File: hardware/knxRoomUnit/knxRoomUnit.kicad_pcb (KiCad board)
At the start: 4 copper layers, 65 x 42 mm, 88 parts, among them J1 esp_prog, J2 JTAG, J3 KNX, P1 ePaper, P2 ePaper FL, Q1 S8050, Q2 S8050, Q3 SI1308, SW1 rst, SW2 knx_prog, SW3 ui_up, SW4 ui_dw, SW5 ui_ok, U1 ESP32-WROOM-32, U2 BME280, U3 VCNL4040M3OE, U4 NCN5130MNTWG, Y1 830055951 16MHz

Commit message: Initial hardware commit
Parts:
- removed C10: 1uF, Capacitor_SMD:C_0603_1608Metric
- removed C11: 10uF, Capacitor_SMD:C_0603_1608Metric
- removed the C12 at (126.5, 70.0)
- removed the C13 at (110.9, 71.5)
- removed the C14 at (110.9, 65.2)
- removed C4: 47nF, Capacitor_SMD:C_0603_1608Metric
- removed C5, C7, C8: 100nF, Capacitor_SMD:C_0603_1608Metric
- removed C6: 220nF, Capacitor_SMD:C_0603_1608Metric
- removed C9: 47uF, Capacitor_SMD:C_Elec_6.3x5.4
- removed D2: SS16, Diode_SMD:D_SMA
- removed the D3 at (142.9, 65.5)
- removed the J2 at (113.6, 46.6)
- removed JP1: UC2, Jumper:SolderJumper-3_P1.3mm_Bridged12_Pad1.0x1.5mm
- removed JP2: UC1, Jumper:SolderJumper-3_P1.3mm_Bridged12_Pad1.0x1.5mm
- removed L1: 220uH, Inductor_SMD:L_Wuerth_MAPI-3020
- removed the R11 at (115.5, 75.9)
- removed the R12 at (123.4, 65.8)
- removed the R13 at (114.2, 62.3)
- removed the R14 at (109.5, 73.6)
- removed the R15 at (109.5, 77.0)
- removed the R16 at (116.3, 62.3)
- removed the R17 at (118.5, 62.3)
- removed Y1: 830055951 16MHz, WE-XTAL:WE-XTAL_CFPX-180
- added GN1: OpenKNX_BCU, OpenKNX:NanoBCU_PinHeader_SMD_low_profile, F.Cu at (128.1, 74.3)
- added R23: 8.2k, Resistor_SMD:R_0603_1608Metric, F.Cu at (83.1, 68.3)
- D3: renamed from D1; value ui_led -> UI
- J1: renamed from J3; footprint Ettinger:13.14.125 -> OpenKNX:KNX_Connector
- J2: renamed from J1; value esp_prog -> PROG
- R10: renamed from R3; footprint Resistor_SMD:R_0402_1005Metric -> Resistor_SMD:R_0603_1608Metric
- R11: renamed from R1; footprint Resistor_SMD:R_0402_1005Metric -> Resistor_SMD:R_0603_1608Metric
- R12: renamed from R4; footprint Resistor_SMD:R_0402_1005Metric -> Resistor_SMD:R_0603_1608Metric
- R13: renamed from R8; footprint Resistor_SMD:R_0402_1005Metric -> Resistor_SMD:R_0603_1608Metric
- R14: renamed from R5; footprint Resistor_SMD:R_0402_1005Metric -> Resistor_SMD:R_0603_1608Metric
- R15: renamed from R6; footprint Resistor_SMD:R_0402_1005Metric -> Resistor_SMD:R_0603_1608Metric
- R16: renamed from R9; footprint Resistor_SMD:R_0402_1005Metric -> Resistor_SMD:R_0603_1608Metric
- R17: renamed from R10; footprint Resistor_SMD:R_0402_1005Metric -> Resistor_SMD:R_0603_1608Metric
- R18: renamed from R7; footprint Resistor_SMD:R_0402_1005Metric -> Resistor_SMD:R_0603_1608Metric
- R19: renamed from R18; footprint Resistor_SMD:R_0402_1005Metric -> Resistor_SMD:R_0603_1608Metric
- R20: renamed from R19; footprint Resistor_SMD:R_0402_1005Metric -> Resistor_SMD:R_0603_1608Metric
- R21: renamed from R20; footprint Resistor_SMD:R_0402_1005Metric -> Resistor_SMD:R_0603_1608Metric
- R22: renamed from R21; footprint Resistor_SMD:R_0402_1005Metric -> Resistor_SMD:R_0603_1608Metric
- R24: renamed from R22; footprint Resistor_SMD:R_0402_1005Metric -> Resistor_SMD:R_0603_1608Metric
- R25: renamed from R23; footprint Resistor_SMD:R_0402_1005Metric -> Resistor_SMD:R_0603_1608Metric
- R26: renamed from R24; footprint Resistor_SMD:R_0402_1005Metric -> Resistor_SMD:R_0603_1608Metric
- R30: renamed from R26; footprint Resistor_SMD:R_0402_1005Metric -> Resistor_SMD:R_0603_1608Metric
- R31: renamed from R27; footprint Resistor_SMD:R_0402_1005Metric -> Resistor_SMD:R_0603_1608Metric
- R9: renamed from R2; footprint Resistor_SMD:R_0402_1005Metric -> Resistor_SMD:R_0603_1608Metric
- SW2: renamed from SW3; value ui_up -> UI_UP
- SW3: renamed from SW2; value knx_prog -> KNX_PROG
- SW4: value ui_dw -> UI_DW
- SW5: value ui_ok -> UI_OK
- U4: value NCN5130MNTWG -> SHT31-DIS; footprint ON_Semiconductor:CASE485AU−01 -> Sensor_Humidity:Sensirion_DFN-8-1EP_2.5x2.5mm_P0.5mm_EP1.1x1.7mm
- moved U4 34.5 mm to (83.9, 65.3), turned to 0 degrees
- moved J1 5.31 mm to (147.0, 71.6), turned to 0 degrees
- moved C22 3.75 mm to (115.5, 49.5)
- moved C24 3.75 mm to (113.0, 49.5)
- moved C25 3.75 mm to (110.5, 49.5)
- moved C26 3.75 mm to (115.5, 53.9)
- moved C28 3.75 mm to (113.0, 53.9)
- moved C30 3.75 mm to (110.5, 53.9)
- moved R1 3.75 mm to (120.3, 58.4), turned to 180 degrees
- moved R18 2.66 mm to (132.2, 38.4)
- moved D3 2.60 mm to (129.0, 38.4)
- moved C14 2.28 mm to (138.3, 38.4)
- moved R11 2.25 mm to (135.3, 38.4)
- moved C13 2.19 mm to (141.4, 38.4), turned to 0 degrees
- moved C12 1.59 mm to (144.4, 38.4), turned to 0 degrees
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- renumbered C1 to C12, C2 to C13, C3 to C14, C24 to C20, C25 to C22, C20 to C23, C26 to C24, C27 to C25, C28 to C26, C22 to C27, C29 to C28, C23 to C29, P2 to P1, P1 to P2, R30 to R1, R28 to R27, R29 to R28, R25 to R29, U1 to U2, U2 to U3, U3 to U5
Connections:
- P1 pad 2: (no net) -> unconnected-(P1-Pin_2-Pad2)
- P1 pad 3: (no net) -> unconnected-(P1-Pin_3-Pad3)
- P1 pad 4: (no net) -> unconnected-(P1-Pin_4-Pad4)
- P2 pad 1: (no net) -> unconnected-(P2-Pin_1-Pad1)
- P2 pad 6: (no net) -> unconnected-(P2-Pin_6-Pad6)
- P2 pad 7: (no net) -> unconnected-(P2-Pin_7-Pad7)
- U2 pad 13: JTAG_TMS -> unconnected-(U2-IO14-Pad13)
- U2 pad 14: JTAG_TDI -> unconnected-(U2-IO12-Pad14)
- U2 pad 16: JTAG_TCK -> unconnected-(U2-IO13-Pad16)
- U2 pad 17: (no net) -> unconnected-(U2-SHD/SD2-Pad17)
- U2 pad 18: (no net) -> unconnected-(U2-SWP/SD3-Pad18)
- U2 pad 19: (no net) -> unconnected-(U2-SCS/CMD-Pad19)
- U2 pad 20: (no net) -> unconnected-(U2-SCK/CLK-Pad20)
- U2 pad 21: (no net) -> unconnected-(U2-SDO/SD0-Pad21)
- U2 pad 22: (no net) -> unconnected-(U2-SDI/SD1-Pad22)
- U2 pad 23: JTAG_TDO -> KNX_SAVE
- U2 pad 32: (no net) -> unconnected-(U2-NC-Pad32)
- U2 pad 4: (no net) -> unconnected-(U2-SENSOR_VP-Pad4)
- U2 pad 5: (no net) -> unconnected-(U2-SENSOR_VN-Pad5)
- U4 pad 1: GND -> unconnected-(U4-SDA-Pad1)
- U4 pad 2: GND -> unconnected-(U4-ADDR-Pad2)
- U4 pad 3: /KNX/TXO -> unconnected-(U4-ALERT-Pad3)
- U4 pad 4: /KNX/CCP -> unconnected-(U4-SCL-Pad4)
- U4 pad 5: /KNX/CAV -> unconnected-(U4-VDD-Pad5)
- U4 pad 6: /KNX/VBUS1 -> unconnected-(U4-~{RESET}-Pad6)
- U4 pad 7: /KNX/CEQ1 -> unconnected-(U4-R-Pad7)
- U4 pad 8: /KNX/CEQ2 -> Net-(U4-VSS-Pad8)
- U4 pad 9: /KNX/VFILT -> Net-(U4-VSS-Pad8)
- U5 pad 3: Net-(C17-Pad1) -> Net-(R23-Pad2)
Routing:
- net Net-(U2-IO35): track 0.00 -> 33.2 mm, vias 0 -> 1
- net ESP_RX: track 0.00 -> 31.4 mm, vias 0 -> 1
- net ESP_TX: track 0.00 -> 31.0 mm, vias 0 -> 1
- net +3V3: track 0.00 -> 29.1 mm, vias 0 -> 2
- net ESP_EN: track 0.00 -> 28.8 mm, vias 0 -> 2
- net KNX_RX: track 0.00 -> 22.7 mm
- net KNX_SAVE: track 0.00 -> 22.5 mm, vias 0 -> 2
- net KNX_TX: track 0.00 -> 19.8 mm
- net Net-(GN1-KNX+): track 0.00 -> 19.2 mm
- net Net-(J2-Pin_5): track 0.00 -> 11.3 mm, vias 0 -> 2
- net Net-(J2-Pin_4): track 0.00 -> 7.53 mm
- net Net-(U2-IO32): track 0.00 -> 5.72 mm
- net I2C_SDA: track 0.00 -> 4.28 mm
- net I2C_SCK: track 0.00 -> 4.14 mm
- net VCNL4040_INT: track 0.00 -> 3.92 mm
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- added copper zone on B.Cu, net GND
- added copper zone on F.Cu, net GND

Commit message: Hardware Update
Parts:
- moved C25 5.01 mm to (115.5, 49.5)
- moved C22 4.89 mm to (110.6, 49.5)
- moved R26 1.03 mm to (136.4, 63.1), turned to 90 degrees
- moved R10 0.74 mm to (121.5, 49.6)
- moved R12 0.55 mm to (142.7, 63.1), turned to 90 degrees
- moved R14 0.50 mm to (139.0, 63.1), turned to 90 degrees
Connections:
- R13 pad 2: Net-(R13-Pad2) -> Net-(U2-IO35)
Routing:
- net /ePaper/PREVGL: track 0.00 -> 30.6 mm
- net Net-(P2-Pin_5): track 0.00 -> 20.7 mm, vias 0 -> 2
- net +3V3: track 29.1 -> 48.8 mm
- net Net-(P2-Pin_4): track 0.00 -> 18.8 mm, vias 0 -> 2
- net Net-(P2-Pin_19): track 0.00 -> 17.6 mm, vias 0 -> 2
- net Net-(C19-Pad1): track 0.00 -> 17.5 mm
- net Net-(P2-Pin_20): track 0.00 -> 17.3 mm, vias 0 -> 2
- net Net-(P2-Pin_22): track 0.00 -> 16.7 mm, vias 0 -> 2
- net /ePaper/PREVGH: track 0.00 -> 13.5 mm
- net Net-(P2-Pin_24): track 0.00 -> 12.2 mm
- net Net-(P2-Pin_18): track 0.00 -> 12.2 mm, vias 0 -> 2
- net Net-(P1-Pin_1): track 0.00 -> 11.7 mm
- net Net-(D6-A): track 0.00 -> 9.93 mm
- net /ePaper/RESE: track 0.00 -> 9.92 mm
- net /ePaper/GDR: track 0.00 -> 8.83 mm
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
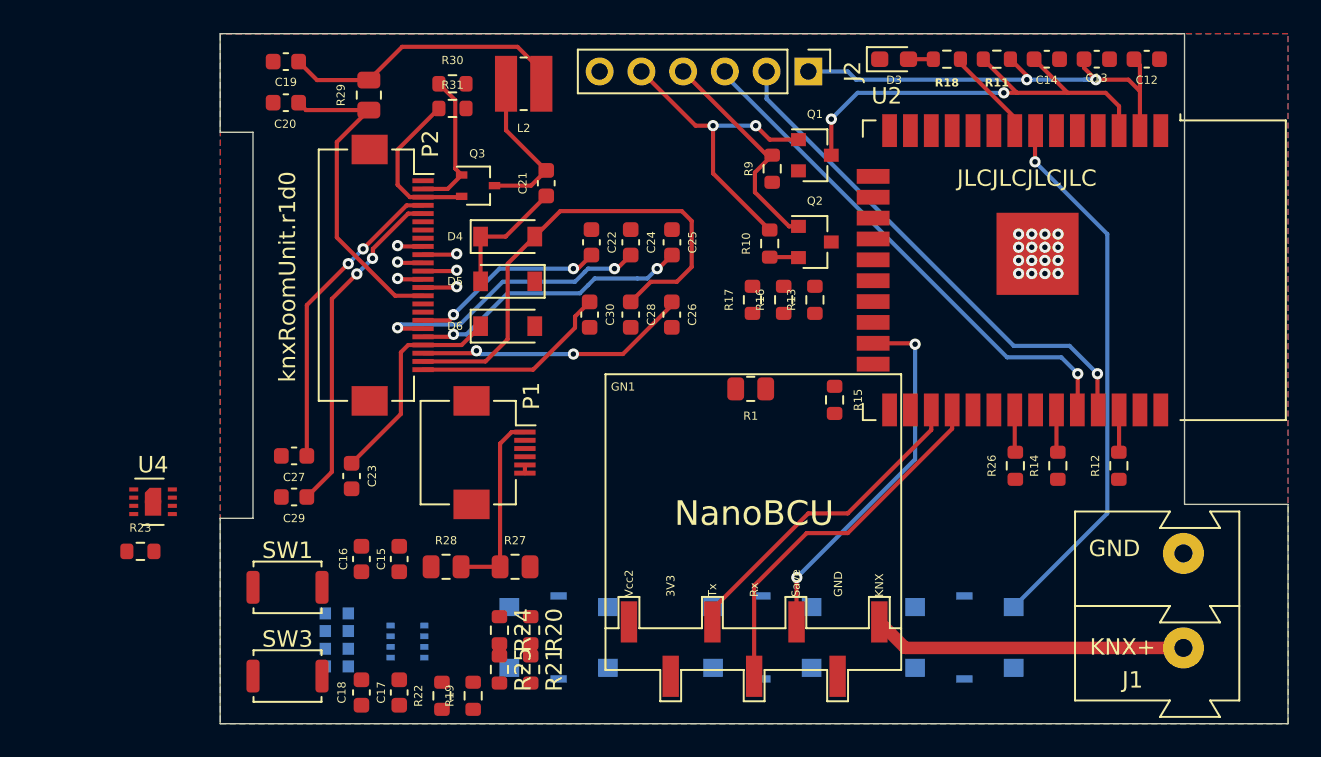
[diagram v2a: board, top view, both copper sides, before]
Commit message: Updated sensors
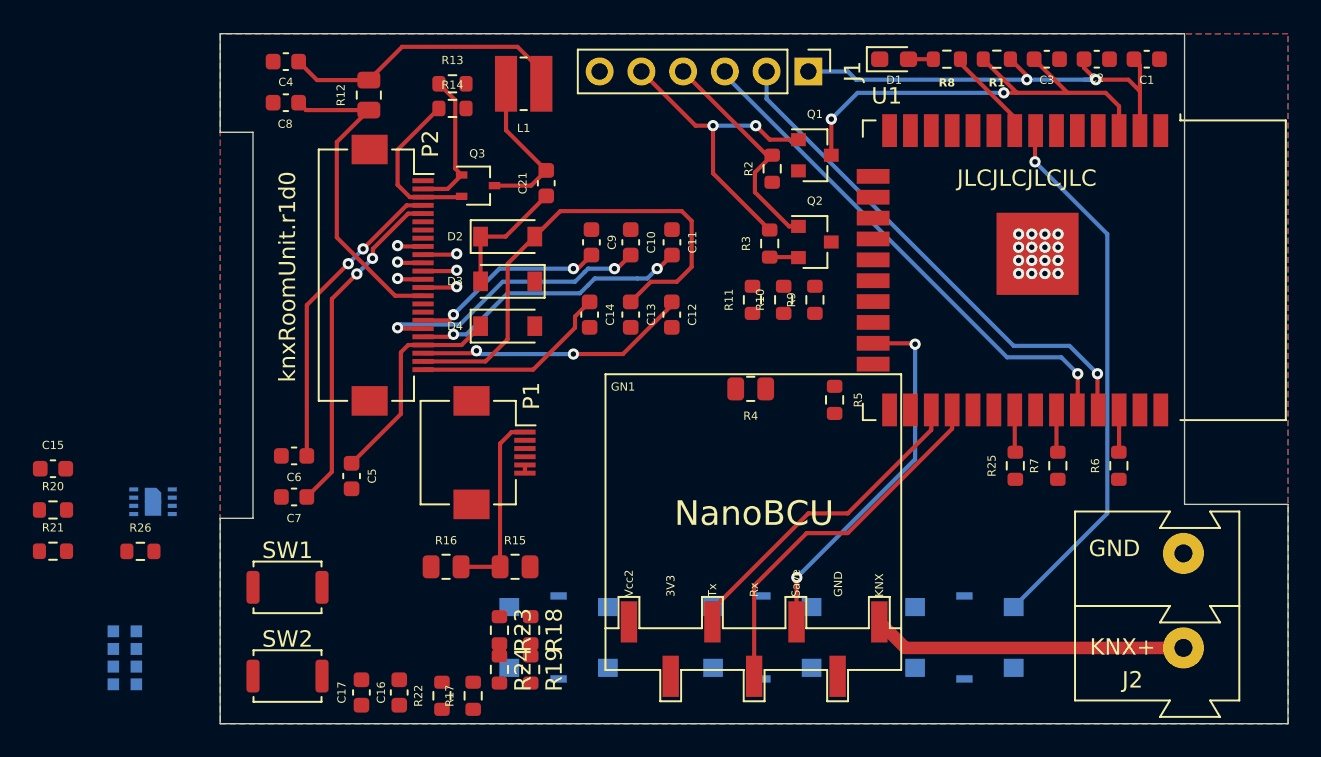
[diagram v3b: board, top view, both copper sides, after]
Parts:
- removed the C16 at (96.6, 68.8)
- removed U5: VCNL4040M3OE, libs:VISHAY_VCNL4040_4X2X1.1
- added R20: 0, Resistor_SMD:R_0603_1608Metric, F.Cu at (77.8, 65.8)
- added R21: 2.2k, Resistor_SMD:R_0603_1608Metric, F.Cu at (77.8, 68.3)
- U2: renamed from U4; moved to B.Cu
- U3: value BME280 -> VCNL4040M3OE; footprint Package_LGA:Bosch_LGA-8_2.5x2.5mm_P0.65mm_ClockwisePinNumbering -> VCNL4040M3OE:VISHAY_VCNL4040_4X2X1.1
- moved C15 21.8 mm to (77.8, 63.3), turned to 0 degrees
- moved U3 17.2 mm to (82.2, 74.8), turned to 180 degrees
- turned U2 to 180 degrees
- renumbered C12 to C1, C24 to C10, C25 to C11, C26 to C12, C28 to C13, C30 to C14, C17 to C16, C18 to C17, C13 to C2, C14 to C3, C19 to C4, C23 to C5, C27 to C6, C29 to C7, C20 to C8, C22 to C9, D3 to D1, D4 to D2, D5 to D3, D6 to D4, J2 to J1, J1 to J2, L2 to L1, R11 to R1, R16 to R10, R17 to R11, R29 to R12, R30 to R13, R31 to R14, R27 to R15, R28 to R16, R19 to R17, R20 to R18, R21 to R19, R9 to R2, R24 to R23, R25 to R24, R26 to R25, R23 to R26, R10 to R3, R1 to R4, R15 to R5, R12 to R6, R14 to R7, R18 to R8, R13 to R9, SW3 to SW2, SW2 to SW3, U2 to U1
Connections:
- C15 pad 1: Net-(U3-CSB) -> Net-(U2-VDD)
- C16 pad 1: Net-(C17-Pad1) -> Net-(C16-Pad1)
- C17 pad 1: Net-(C17-Pad1) -> Net-(C16-Pad1)
- R10 pad 2: Net-(U2-IO34) -> Net-(U1-IO34)
- R11 pad 2: Net-(U2-IO33) -> Net-(U1-IO33)
- R17 pad 2: Net-(U3-CSB) -> Net-(U2-VDD)
- R18 pad 1: Net-(U3-SCK) -> Net-(U2-SCL)
- R19 pad 1: Net-(U3-SDI) -> Net-(U2-SDA)
- R22 pad 2: Net-(C17-Pad1) -> Net-(C16-Pad1)
- R23 pad 1: Net-(R24-Pad1) -> Net-(R23-Pad1)
- R24 pad 1: Net-(R25-Pad1) -> Net-(R24-Pad1)
- R25 pad 1: Net-(R26-Pad1) -> Net-(R25-Pad1)
- R26 pad 1: Net-(C17-Pad1) -> Net-(C16-Pad1)
- R26 pad 2: Net-(R23-Pad2) -> Net-(R26-Pad2)
- R9 pad 2: Net-(U2-IO35) -> Net-(U1-IO35)
- U1 pad 6: Net-(U2-IO34) -> Net-(U1-IO34)
- U1 pad 7: Net-(U2-IO35) -> Net-(U1-IO35)
- U1 pad 9: Net-(U2-IO33) -> Net-(U1-IO33)
- U2 pad 1: unconnected-(U4-SDA-Pad1) -> Net-(U2-SDA)
- U2 pad 2: unconnected-(U4-ADDR-Pad2) -> GND
- U2 pad 3: unconnected-(U4-ALERT-Pad3) -> Net-(U2-ALERT)
- U2 pad 4: unconnected-(U4-SCL-Pad4) -> Net-(U2-SCL)
- U2 pad 5: unconnected-(U4-VDD-Pad5) -> Net-(U2-VDD)
- U2 pad 6: unconnected-(U4-~{RESET}-Pad6) -> Net-(U2-~{RESET})
- U2 pad 7: unconnected-(U4-R-Pad7) -> GND
- U2 pad 8: Net-(U4-VSS-Pad8) -> GND
- U2 pad 9: Net-(U4-VSS-Pad8) -> GND
- U3 pad 2: Net-(U3-CSB) -> Net-(U3-Pad2)
- U3 pad 3: Net-(U3-SDI) -> Net-(R26-Pad2)
- U3 pad 4: Net-(U3-SCK) -> Net-(C16-Pad1)
- U3 pad 5: GND -> Net-(U3-Pad2)
- U3 pad 6: Net-(U3-CSB) -> Net-(R25-Pad1)
- U3 pad 7: GND -> Net-(R24-Pad1)
- U3 pad 8: Net-(U3-CSB) -> Net-(R23-Pad1)

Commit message: PCB routing
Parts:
- added D0: PWR, LED_SMD:LED_0603_1608Metric_Pad1.05x0.95mm_HandSolder, F.Cu at (131.8, 63.6)
- added R0: 75, Resistor_SMD:R_0603_1608Metric, F.Cu at (131.8, 66.0)
- R17, R18, R19, R20, R22, R23, R24, R25: footprint Resistor_SMD:R_0603_1608Metric -> Resistor_SMD:R_0201_0603Metric
- SW1: value rst -> RESET
- SW2: value KNX_PROG -> KNX
- moved R25 40.4 mm to (96.2, 68.0), turned to 0 degrees
- moved SW2 39.3 mm to (115.8, 44.5), turned to -90 degrees
- moved SW1 32.1 mm to (111.1, 44.6), turned to -90 degrees
- moved C15 27.3 mm to (101.7, 76.4)
- moved R20 23.2 mm to (100.8, 69.1), turned to 90 degrees
- moved R21 22.0 mm to (98.3, 76.4)
- moved U2 18.4 mm to (100.1, 74.0)
- moved R24 12.0 mm to (96.2, 67.2), turned to 0 degrees
- moved R26 12.0 mm to (94.1, 73.2), turned to 180 degrees
- moved U3 11.9 mm to (94.1, 73.9)
- moved R23 11.0 mm to (96.2, 66.5), turned to 0 degrees
- moved R15 10.7 mm to (109.8, 59.3), turned to -90 degrees
- moved R16 10.0 mm to (109.8, 63.3), turned to 90 degrees
- moved R19 9.36 mm to (100.0, 69.1), turned to 90 degrees
- moved R17 8.65 mm to (94.8, 78.0), turned to 0 degrees
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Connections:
- U1 pad 13: unconnected-(U1-IO14-Pad13) -> SHT31_ALERT
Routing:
- net +3V3: track 48.8 -> 182.1 mm, vias 2 -> 14
- net I2C_SCK: track 2.58 -> 54.8 mm, vias 0 -> 2
- net I2C_SDA: track 2.72 -> 49.4 mm, vias 0 -> 4
- net VCNL4040_INT: track 2.59 -> 44.4 mm, vias 0 -> 2
- net EPAPER_DC: track 1.57 -> 42.7 mm, vias 1 -> 2
- net EPAPER_RST: track 2.07 -> 37.9 mm, vias 1 -> 2
- net Net-(U1-IO2): track 0.00 -> 30.2 mm, vias 0 -> 3
- net Net-(U1-IO34): track 0.00 -> 27.2 mm, vias 0 -> 2
- net +3.3VP: track 0.00 -> 24.7 mm, vias 0 -> 2
- net ESP_BOOT: track 0.00 -> 24.6 mm
- net Net-(U1-IO35): track 0.00 -> 22.5 mm, vias 0 -> 2
- net Net-(U1-IO33): track 0.00 -> 19.0 mm, vias 0 -> 2
- net ESP_EN: track 28.8 -> 47.6 mm, vias 2 -> 3
- net GND: track 0.50 -> 18.2 mm, vias 16 -> 39
- net Net-(R25-Pad1): track 0.00 -> 12.0 mm, vias 0 -> 1
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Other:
- outline, holes or cut-outs redrawn

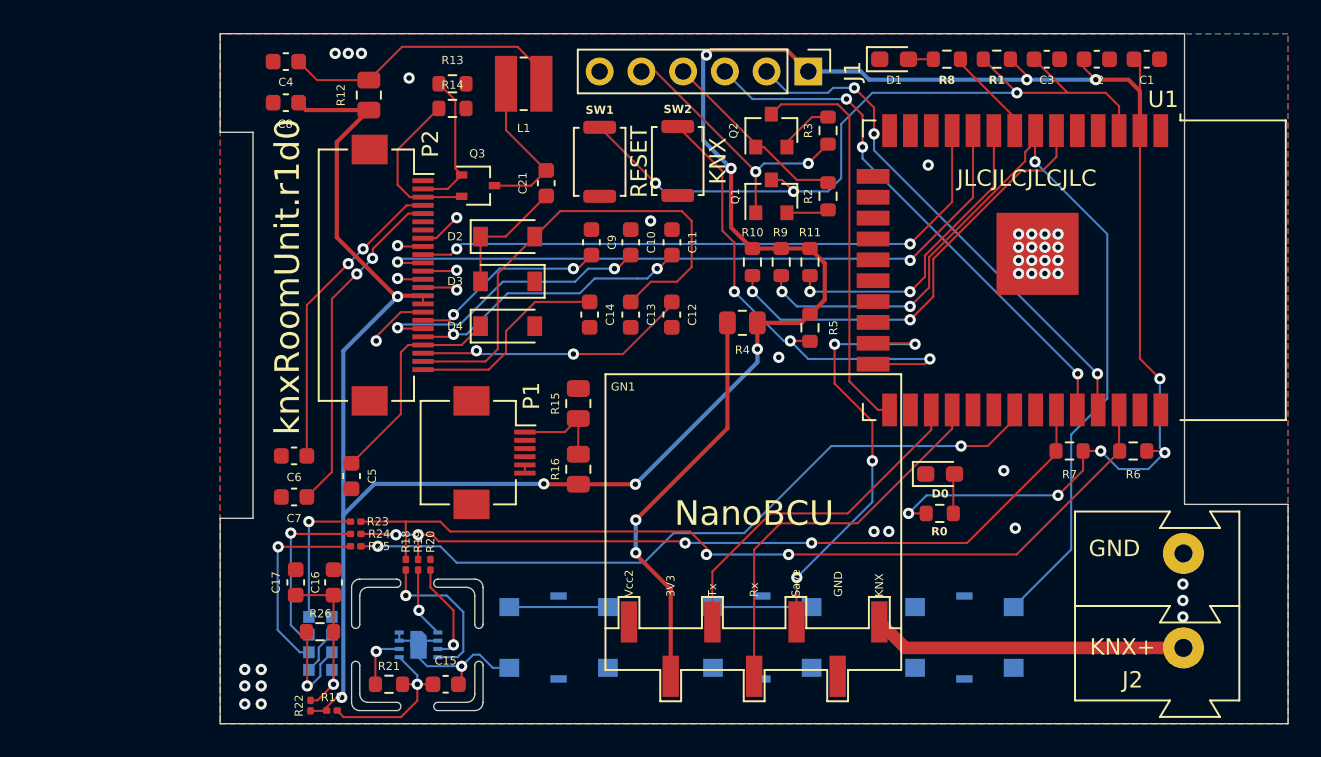
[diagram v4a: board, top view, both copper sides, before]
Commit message: Finished PCB routing
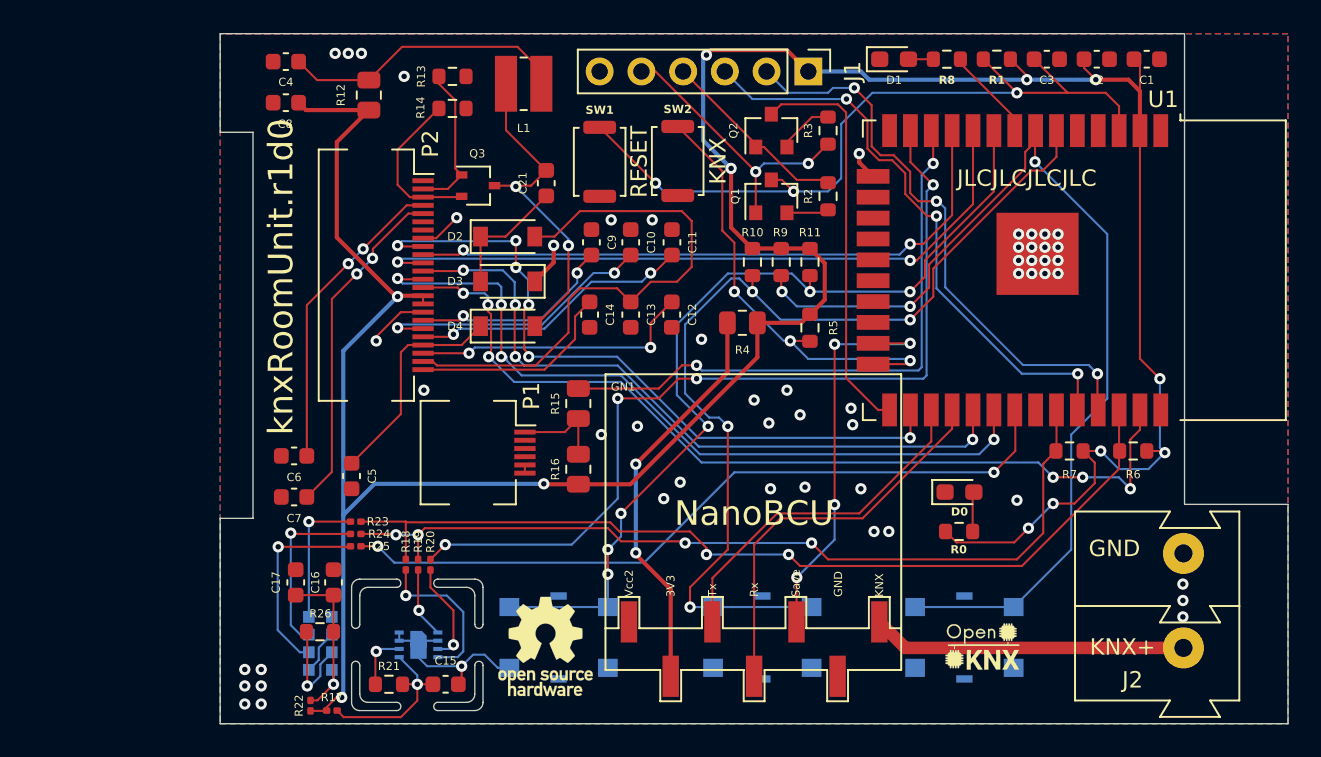
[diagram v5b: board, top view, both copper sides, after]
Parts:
- added G***: LOGO, OpenKNX:OpenKNX_Logo_05x03, F.Cu at (134.4, 74.3)
- added REF**: OSHW-Logo_5.7x6mm_SilkScreen, Symbol:OSHW-Logo_5.7x6mm_SilkScreen, F.Cu at (107.8, 74.1)
- SW3: value UI_UP -> DW; footprint WS-TASV:431151008826 -> 431151008826:431151008826
- SW4: value UI_DW -> OK; footprint WS-TASV:431151008826 -> 431151008826:431151008826
- SW5: value UI_OK -> UP; footprint WS-TASV:431151008826 -> 431151008826:431151008826
- moved D0 1.61 mm to (133.0, 64.7)
- moved R0 1.61 mm to (133.0, 67.1)
- moved R13 0.45 mm to (102.1, 39.4)
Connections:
- SW3 pad 1: Net-(R13-Pad2) -> Net-(U1-IO35)
- SW3 pad 3: Net-(U2-IO35) -> Net-(U1-IO35)
- SW4 pad 1: Net-(U2-IO34) -> Net-(U1-IO34)
- SW4 pad 3: Net-(U2-IO34) -> Net-(U1-IO34)
- SW5 pad 1: Net-(U2-IO33) -> Net-(U1-IO33)
- SW5 pad 3: Net-(U2-IO33) -> Net-(U1-IO33)
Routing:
- net SHT31_ALERT: track 0.00 -> 54.1 mm, vias 0 -> 4
- net EPAPER_SDI: track 2.04 -> 55.7 mm, vias 1 -> 6
- net EPAPER_CLK: track 1.57 -> 47.1 mm, vias 1 -> 4
- net EPAPER_BUSY: track 1.57 -> 43.4 mm, vias 1 -> 6
- net EPAPER_CS: track 2.07 -> 42.5 mm, vias 1 -> 4
- net Net-(U1-IO35): track 22.5 -> 61.7 mm, vias 2 -> 3
- net EPAPER_FL: track 0.00 -> 36.4 mm, vias 0 -> 2
- net Net-(U1-IO33): track 19.0 -> 55.3 mm, vias 2 -> 6
- net Net-(U2-IO35): track 33.1 -> 0.00 mm, vias 1 -> 0
- net Net-(U1-IO34): track 27.2 -> 59.5 mm, vias 2 -> 4
- net Net-(D4-A): track 9.93 -> 20.6 mm, vias 0 -> 2
- net Net-(U2-IO34): track 6.00 -> 0.00 mm
- net Net-(U2-IO33): track 6.00 -> 0.00 mm
- net GND: track 18.2 -> 22.6 mm, vias 39 -> 54
- net /ePaper/PREVGL: track 30.6 -> 34.2 mm
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
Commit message: Production adjustments
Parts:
- removed G***: LOGO, OpenKNX:OpenKNX_Logo_05x03
- removed REF**: OSHW-Logo_5.7x6mm_SilkScreen, Symbol:OSHW-Logo_5.7x6mm_SilkScreen
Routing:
- net GND: track 22.6 -> 58.2 mm, vias 54 -> 69
- net ESP_EN: track 47.6 -> 37.2 mm
- net +3V3: track 180.1 -> 183.7 mm

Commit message: Fixed HW production files
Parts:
- added G***: LOGO, OpenKNX:OpenKNX_Logo_05x03, F.Cu at (134.3, 76.7)
- added REF**: OSHW-Logo2_7.3x6mm_SilkScreen, Symbol:OSHW-Logo2_7.3x6mm_SilkScreen, F.Cu at (134.3, 71.0)
- moved R22 12.1 mm to (105.6, 77.5), turned to 180 degrees
- moved R17 10.9 mm to (105.6, 76.5), turned to 180 degrees
- turned R1 to 0 degrees
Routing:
- net +3V3: track 183.7 -> 171.3 mm
- net Net-(C16-Pad1): track 10.4 -> 21.6 mm
- net ESP_EN: track 37.2 -> 45.9 mm, vias 3 -> 4
- net GND: track 58.2 -> 60.0 mm
- net Net-(R26-Pad2): track 6.18 -> 7.69 mm
- net Net-(U2-VDD): track 10.6 -> 11.7 mm
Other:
- copper layers 4 -> 2

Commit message: Fixed HW production files
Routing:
- net Net-(R26-Pad2): track 7.69 -> 10.2 mm
- net EPAPER_BUSY: track 43.4 -> 44.2 mm
- net EPAPER_SDI: track 55.7 -> 56.2 mm, vias 6 -> 4
